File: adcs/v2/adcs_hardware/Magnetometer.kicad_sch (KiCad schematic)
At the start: 1 part, among them U3 LIS2MDL

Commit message: magnetometer subsheet wiring
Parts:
- added C19, C2: 100n, Package_DIP:DIP-8_W7.62mm, symbol Device:C_Small_US
- added C20: 1u, Package_DIP:DIP-8_W7.62mm, symbol Device:C_Small_US
- added C21: 220n, Package_DIP:DIP-8_W7.62mm, symbol Device:C_Small_US
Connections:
- net GND: now also C19.2, C2.2, C20.2, C21.2
- net SCL: now reaches U3.1 (SCL/SPC)
- net +1V8: now reaches U3.10 (Vdd_IO)
- net +1V8: now also U3.3 (~{CS}), U3.9 (Vdd), C19.1, C2.1, C20.1
- net SDA: now reaches U3.4 (SDA/SDI/SDO)
- net at U3.5 (C1): now also C21.1
- net MNT-INT: now reaches U3.7 (DRDY)
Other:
- moved on the sheet: U3

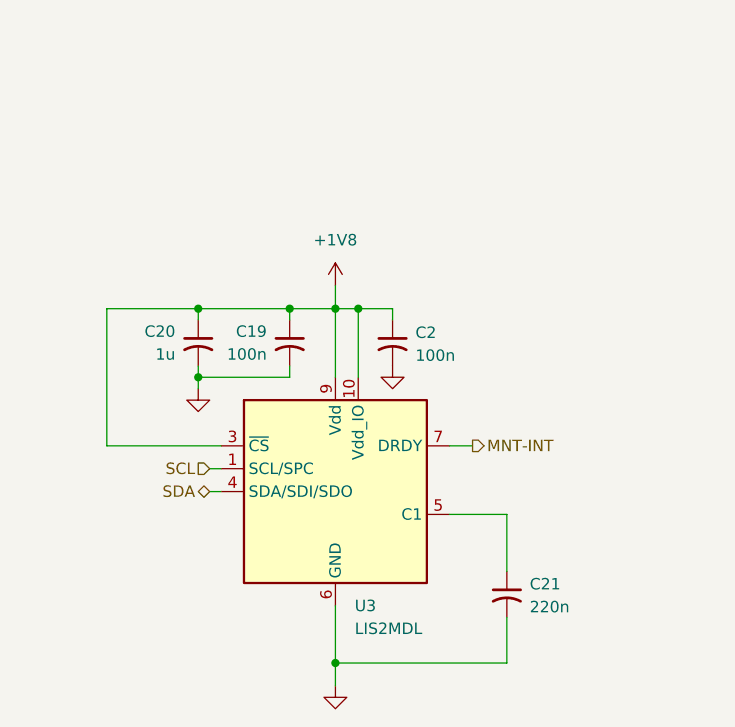
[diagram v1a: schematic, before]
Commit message: begin adding GPIOs
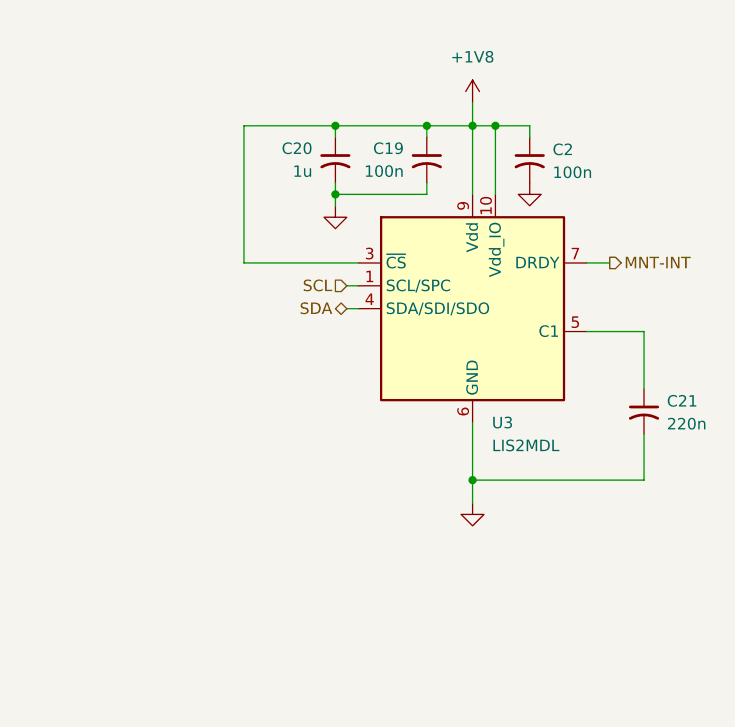
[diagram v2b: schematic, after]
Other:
- moved on the sheet: C19, C2, C20, C21, U3

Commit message: added no-connects, adcs mcu
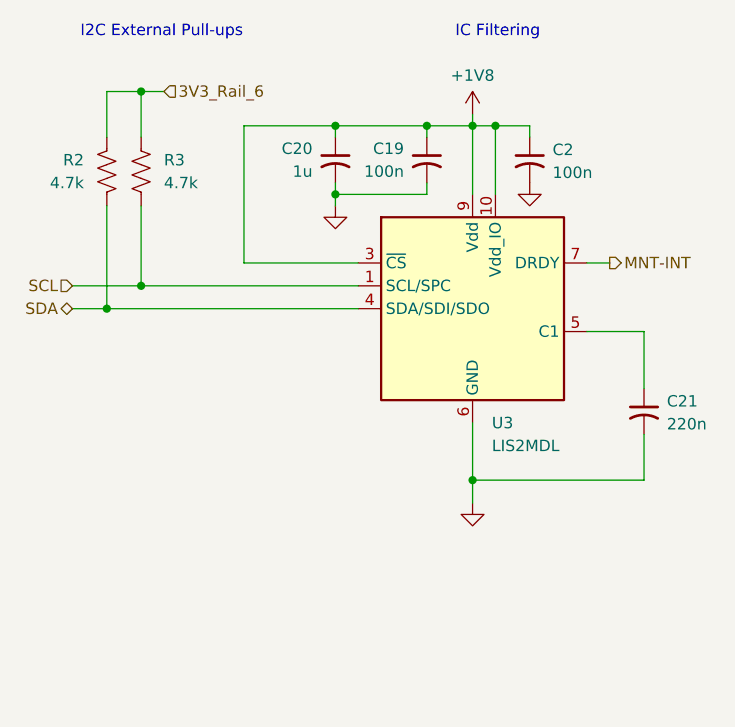
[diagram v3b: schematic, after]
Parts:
- added R2, R3: 4.7k, Converter_DCDC:Converter_DCDC_RECOM_R-78B-2.0_THT, symbol Device:R_US
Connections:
- net SCL: now also R3.2
- net SDA: now also R2.2
- new net 3V3_Rail_6: R2.1, R3.1
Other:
- note added: "I2C External Pull-ups"
- note added: "IC Filtering"
